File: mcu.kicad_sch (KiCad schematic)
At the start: 11 parts, among them J301 Conn_01x05_Pin, J302 Conn_01x10_Pin, SW301 TS-1088R-02026, SW302 TS-1088R-02026, U301 ESP-12F

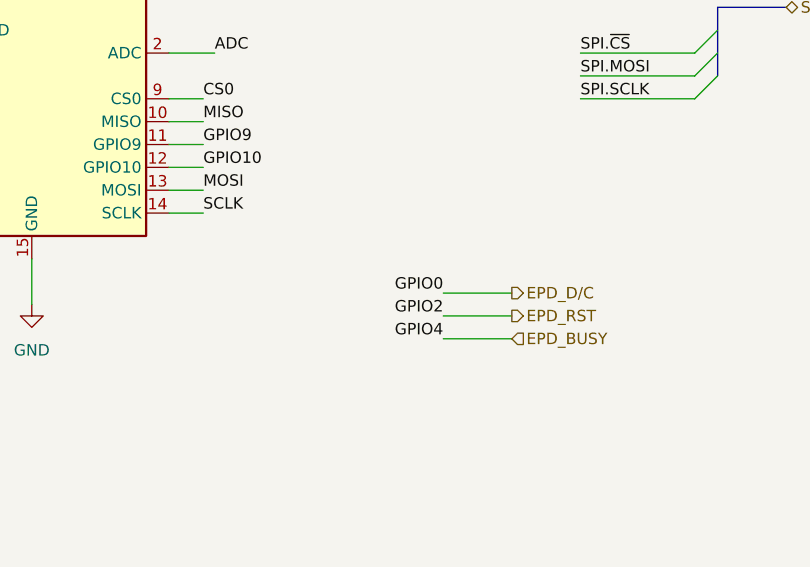
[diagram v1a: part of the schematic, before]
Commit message: Fix using same GPIO for epd D/C and boot
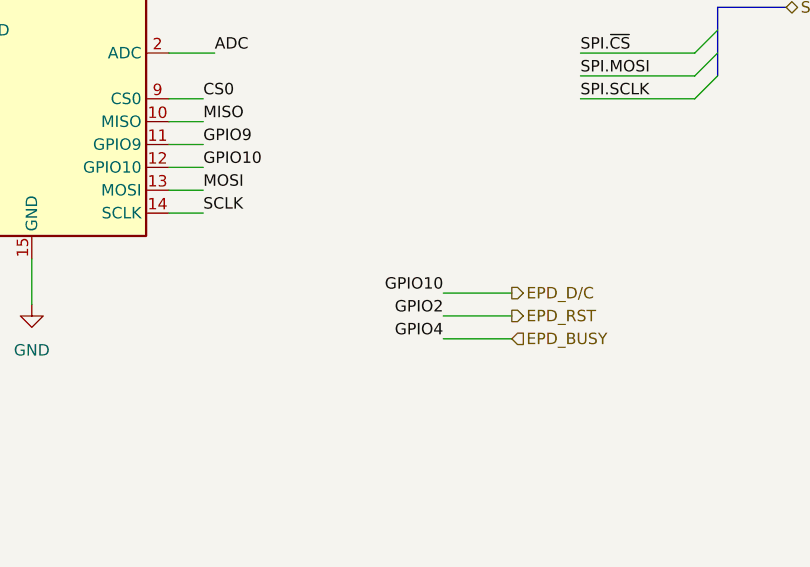
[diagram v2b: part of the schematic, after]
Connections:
- net GPIO10 is gone; now on net EPD_D/C: J302.10 (Pin_10), U301.12 (GPIO10)
- net EPD_D/C: no longer J302.6 (Pin_6), R302.2, SW302.2, U301.18 (GPIO0)
- new net GPIO0: J302.6 (Pin_6), R302.2, SW302.2, U301.18 (GPIO0)
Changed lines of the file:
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@@
 		)
 	)
-	(label "GPIO0"
+	(label "GPIO10"
 		(at 205.74 125.73 180)
 		(effects

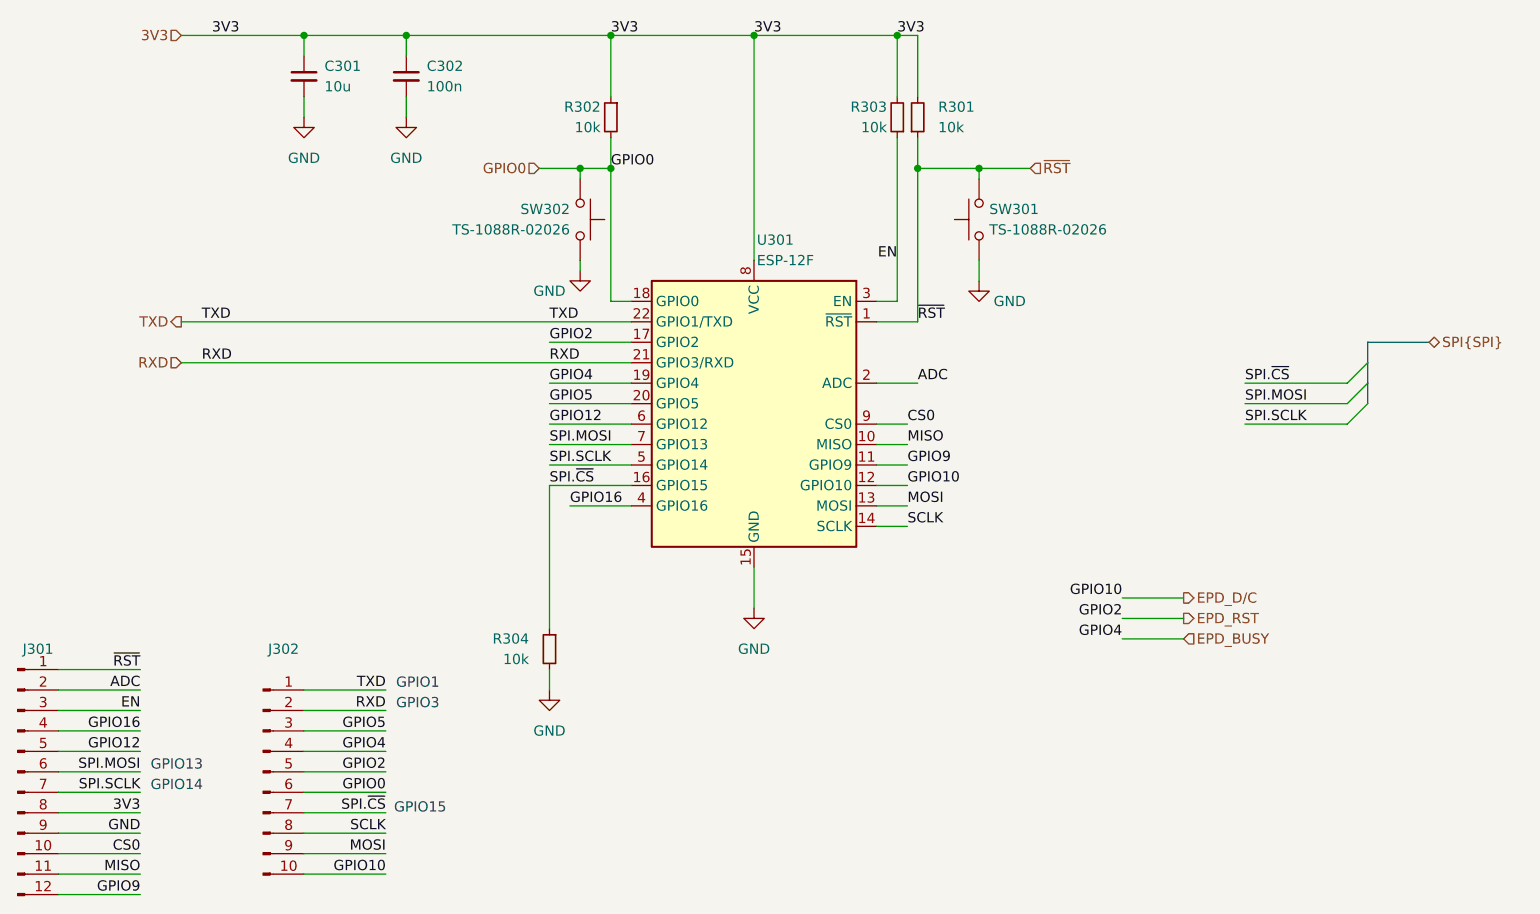
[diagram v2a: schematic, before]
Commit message: Update reference designators to single digit
Fits on the silk better
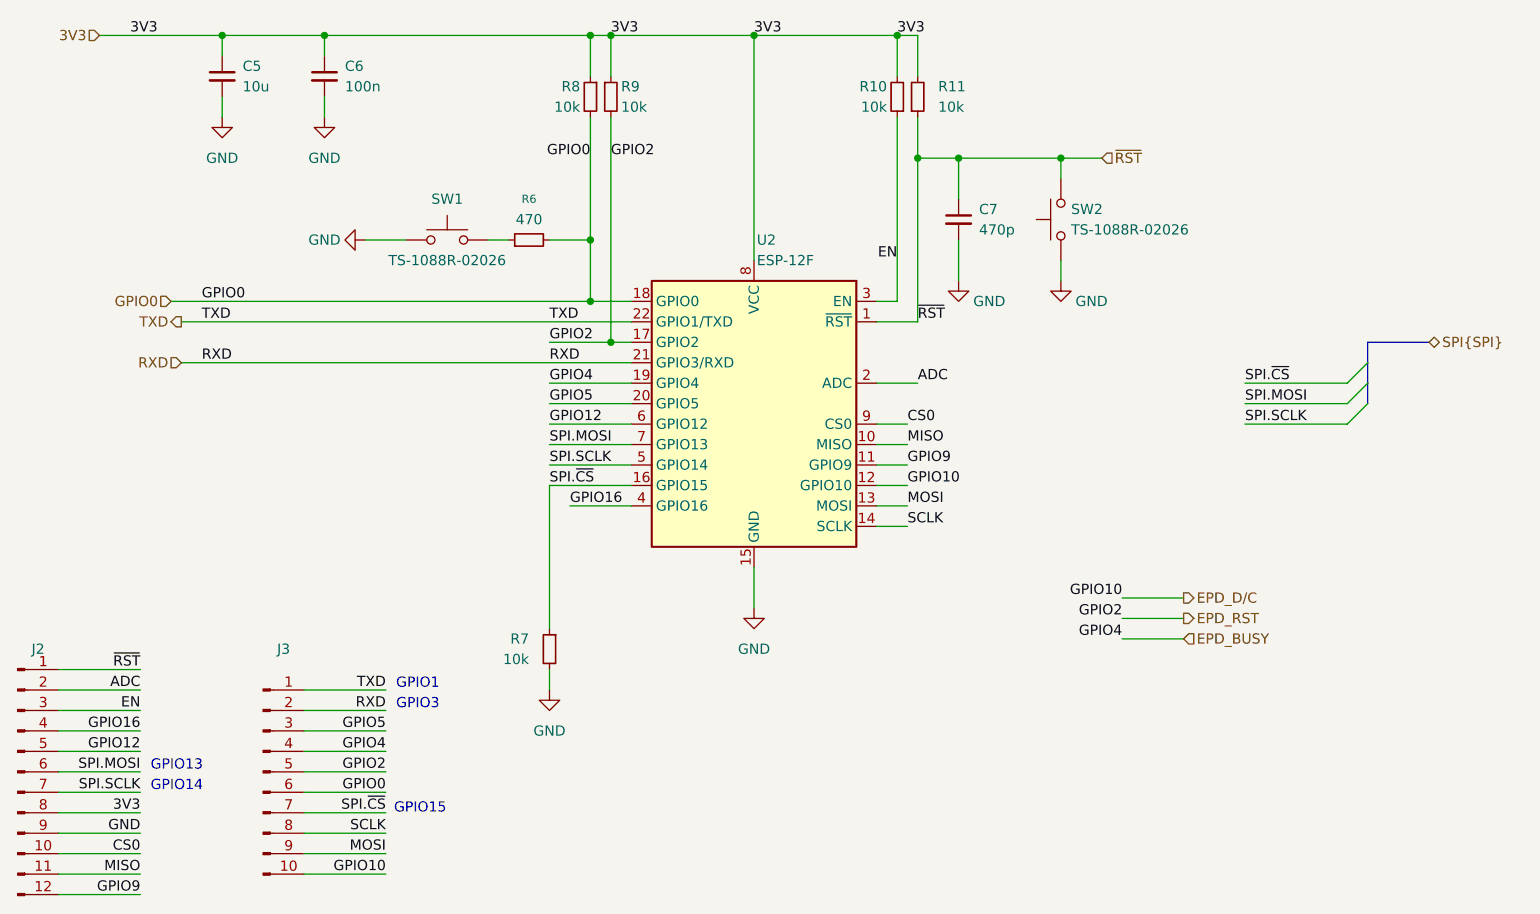
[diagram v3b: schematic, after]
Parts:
- added C7: 470p, Capacitor_SMD:C_0805_2012Metric, symbol Device:C_Small
- added R6: 470, Resistor_SMD:R_0805_2012Metric, symbol Device:R_Small
- added R9: 10k, Resistor_SMD:R_0805_2012Metric, symbol Device:R_Small
- renumbered C301 to C5, C302 to C6, J301 to J2, J302 to J3, R303 to R10, R301 to R11, R304 to R7, R302 to R8, SW302 to SW1, SW301 to SW2, U301 to U2
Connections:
- net 3V3: now also R9.1
- net EPD_RST: now also R9.2
- net GND: now also SW1.2, C7.2; no longer SW1.1
- net GPIO0: now also R6.2; no longer SW1.2
- net ~{RST}: now also C7.1
- new net: R6.1, SW1.1
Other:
- moved on the sheet: C5, C6, R10, R11, R8, SW1, SW2

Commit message: Lighthouse
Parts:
- SW1, SW2: footprint youdbetterrun:TS-1088R-02026_SW_SMD_3x4mm -> bedroom_lights:TS-1088R-02026_SW_SMD_3x4mm
- U2: symbol youdbetterrun:ESP-12F -> bedroom_lights:ESP-12F
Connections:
- net EPD_BUSY renamed GPIO4
- net EPD_D/C renamed CSO1
- net EPD_RST renamed GPIO2
- net GPIO12 renamed CSO2
- net GPIO16 renamed LSS2
- net GPIO9 renamed LSS1
- net SPI.MOSI renamed GPIO13
- net SPI.SCLK renamed GPIO14
- net SPI.~{CS} renamed GPIO15
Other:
- note removed: "GPIO13"
- note removed: "GPIO14"
- note removed: "GPIO15"
- company: (none) -> Marcel Robitaille
- title: (none) -> MCU

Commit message: ERC
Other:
- note added: "GPIO10"
- note added: "GPIO12"
- note added: "GPIO16"
- note added: "GPIO9"
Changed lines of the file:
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@@
 		(company "Marcel Robitaille")
+	)
+	(text "GPIO16"
+		(exclude_from_sim no)
+		(at 213.36 114.3 0)
+		(effects
+			(font
+				(size 1.27 1.27)
+			)
+			(justify left bottom)
+		)
 	)
 	(text "GPIO1"
@@
 		)
 	)
+	(text "GPIO10"
+		(exclude_from_sim no)
+		(at 213.36 104.14 0)
+		(effects
+			(font
+				(size 1.27 1.27)
+			)
+			(justify left bottom)
+		)
+	)
+	(text "GPIO12"
+		(exclude_from_sim no)
+		(at 213.36 106.68 0)
+		(effects
+			(font
+				(size 1.27 1.27)
+			)
+			(justify left bottom)
+		)
+	)
 	(text "GPIO3"
 		(exclude_from_sim no)
 		(at 115.57 139.7 0)
+		(effects
+			(font
+				(size 1.27 1.27)
+			)
+			(justify left bottom)
+		)
+	)
+	(text "GPIO9"
+		(exclude_from_sim no)
+		(at 213.36 111.76 0)
 		(effects
 			(font
@@
 	(wire
 		(pts
-			(xy 213.36 106.68) (xy 218.44 106.68)
+			(xy 213.36 106.68) (xy 223.52 106.68)
 		)
 		(stroke
@@
 	(wire
 		(pts
-			(xy 213.36 114.3) (xy 218.44 114.3)
+			(xy 213.36 114.3) (xy 223.52 114.3)
 		)
 		(stroke
@@
 	(wire
 		(pts
-			(xy 213.36 111.76) (xy 218.44 111.76)
+			(xy 213.36 111.76) (xy 223.52 111.76)
 		)
 		(stroke
@@
 	(wire
 		(pts
-			(xy 213.36 104.14) (xy 218.44 104.14)
+			(xy 213.36 104.14) (xy 223.52 104.14)
 		)
 		(stroke
@@
 		)
 	)
+	(label "LSS1"
+		(at 213.36 111.76 180)
+		(effects
+			(font
+				(size 1.27 1.27)
+			)
+			(justify right bottom)
+		)
+	)
 	(label "SCLK"
 		(at 179.07 116.84 0)
@@
 		)
 	)
-	(label "GPIO12"
-		(at 83.82 144.78 180)
+	(label "CSO2"
+		(at 134.62 104.14 0)
+		(effects
+			(font
+				(size 1.27 1.27)
+			)
+			(justify left bottom)
+		)
+	)
+	(label "CSO1"
+		(at 114.3 160.02 180)
 		(effects
 			(font
@@
 		)
 	)
+	(label "CSO1"
+		(at 179.07 111.76 0)
+		(effects
+			(font
+				(size 1.27 1.27)
+			)
+			(justify left bottom)
+		)
+	)
 	(label "~{RST}"
 		(at 180.34 91.44 0)
@@
 		)
 	)
-	(label "GPIO12"
-		(at 134.62 104.14 0)
-		(effects
-			(font
-				(size 1.27 1.27)
-			)
-			(justify left bottom)
-		)
-	)
 	(label "GPIO2"
 		(at 142.24 71.12 0)
@@
 		)
 	)
+	(label "CSO2"
+		(at 83.82 144.78 180)
+		(effects
+			(font
+				(size 1.27 1.27)
+			)
+			(justify right bottom)
+		)
+	)
 	(label "MOSI"
 		(at 114.3 157.48 180)
@@
 		)
 	)
-	(label "GPIO9"
-		(at 213.36 111.76 180)
-		(effects
-			(font
-				(size 1.27 1.27)
-			)
-			(justify right bottom)
-		)
-	)
 	(label "3V3"
 		(at 83.82 152.4 180)
@@
 		)
 	)
-	(label "GPIO12"
-		(at 213.36 106.68 180)
-		(effects
-			(font
-				(size 1.27 1.27)
-			)
-			(justify right bottom)
-		)
-	)
 	(label "GPIO5"
 		(at 134.62 101.6 0)
@@
 		)
 	)
+	(label "LSS2"
+		(at 137.16 114.3 0)
+		(effects
+			(font
+				(size 1.27 1.27)
+			)
+			(justify left bottom)
+		)
+	)
+	(label "LSS2"
+		(at 213.36 114.3 180)
+		(effects
+			(font
+				(size 1.27 1.27)
+			)
+			(justify right bottom)
+		)
+	)
 	(label "3V3"
 		(at 82.55 55.88 0)
@@
 		)
 	)
-	(label "GPIO10"
-		(at 114.3 160.02 180)
-		(effects
-			(font
-				(size 1.27 1.27)
-			)
-			(justify right bottom)
-		)
-	)
 	(label "GPIO13"
 		(at 83.82 147.32 180)
@@
 		)
 	)
+	(label "LSS2"
+		(at 83.82 142.24 180)
+		(effects
+			(font
+				(size 1.27 1.27)
+			)
+			(justify right bottom)
+		)
+	)
 	(label "CS0"
 		(at 179.07 104.14 0)
@@
 		)
 	)
-	(label "GPIO9"
-		(at 179.07 109.22 0)
-		(effects
-			(font
-				(size 1.27 1.27)
-			)
-			(justify left bottom)
-		)
-	)
 	(label "GND"
 		(at 83.82 154.94 180)
@@
 		)
 	)
-	(label "GPIO9"
-		(at 83.82 162.56 180)
-		(effects
-			(font
-				(size 1.27 1.27)
-			)
-			(justify right bottom)
-		)
-	)
-	(label "GPIO16"
-		(at 213.36 114.3 180)
-		(effects
-			(font
-				(size 1.27 1.27)
-			)
-			(justify right bottom)
-		)
-	)
-	(label "GPIO16"
-		(at 83.82 142.24 180)
+	(label "CSO1"
+		(at 213.36 104.14 180)
 		(effects
 			(font
@@
 		)
 	)
+	(label "CSO2"
+		(at 213.36 106.68 180)
+		(effects
+			(font
+				(size 1.27 1.27)
+			)
+			(justify right bottom)
+		)
+	)
 	(label "MISO"
 		(at 83.82 160.02 180)
@@
 		)
 	)
+	(label "LSS1"
+		(at 83.82 162.56 180)
+		(effects
+			(font
+				(size 1.27 1.27)
+			)
+			(justify right bottom)
+		)
+	)
 	(label "TXD"
 		(at 134.62 91.44 0)
@@
 		)
 	)
-	(label "GPIO10"
-		(at 179.07 111.76 0)
-		(effects
-			(font
-				(size 1.27 1.27)
-			)
-			(justify left bottom)
-		)
-	)
 	(label "GPIO5"
 		(at 114.3 142.24 180)
@@
 		)
 	)
-	(label "GPIO10"
-		(at 213.36 104.14 180)
-		(effects
-			(font
-				(size 1.27 1.27)
-			)
-			(justify right bottom)
-		)
-	)
 	(label "GPIO0"
 		(at 91.44 88.9 0)
@@
 		)
 	)
-	(label "GPIO16"
-		(at 137.16 114.3 0)
-		(effects
-			(font
-				(size 1.27 1.27)
-			)
-			(justify left bottom)
-		)
-	)
 	(label "GPIO14"
 		(at 134.62 109.22 0)
@@
 		)
 	)
+	(label "LSS1"
+		(at 179.07 109.22 0)
+		(effects
+			(font
+				(size 1.27 1.27)
+			)
+			(justify left bottom)
+		)
+	)
 	(label "CS0"
 		(at 83.82 157.48 180)
@@
 	(hierarchical_label "LSS1"
 		(shape output)
-		(at 218.44 111.76 0)
+		(at 223.52 111.76 0)
 		(effects
 			(font
@@
 	(hierarchical_label "LSS2"
 		(shape output)
-		(at 218.44 114.3 0)
+		(at 223.52 114.3 0)
 		(effects
 			(font
@@
 	(hierarchical_label "CSO1"
 		(shape output)
-		(at 218.44 104.14 0)
+		(at 223.52 104.14 0)
 		(effects
 			(font
@@
 	(hierarchical_label "CSO2"
 		(shape output)
-		(at 218.44 106.68 0)
-		(effects
-			(font
+		(at 223.52 106.68 0)
+		(effects
+			(font

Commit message: Renamifications
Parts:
- SW1, SW2: footprint bedroom_lights:TS-1088R-02026_SW_SMD_3x4mm -> lighthouse:TS-1088R-02026_SW_SMD_3x4mm
- U2: symbol bedroom_lights:ESP-12F -> lighthouse:ESP-12F
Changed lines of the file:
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@@
 		)
 		(instances
-			(project "bedroom_lights"
+			(project "lighthouse"
 				(path "/50da2b4e-34b1-4787-8ee6-5d7d17f804f4/81f185f6-8abd-42b2-b2d9-f7e00f67ab8b"
 					(reference "#PWR010")
@@
 		)
 		(instances
-			(project "bedroom_lights"
+			(project "lighthouse"
 				(path "/50da2b4e-34b1-4787-8ee6-5d7d17f804f4/81f185f6-8abd-42b2-b2d9-f7e00f67ab8b"
 					(reference "#PWR012")
@@
 		)
 		(instances
-			(project "bedroom_lights"
+			(project "lighthouse"
 				(path "/50da2b4e-34b1-4787-8ee6-5d7d17f804f4/81f185f6-8abd-42b2-b2d9-f7e00f67ab8b"
 					(reference "#PWR014")
@@
 		)
 		(instances
-			(project "bedroom_lights"
+			(project "lighthouse"
 				(path "/50da2b4e-34b1-4787-8ee6-5d7d17f804f4/81f185f6-8abd-42b2-b2d9-f7e00f67ab8b"
 					(reference "C6")
@@
 		)
 		(instances
-			(project "bedroom_lights"
+			(project "lighthouse"
 				(path "/50da2b4e-34b1-4787-8ee6-5d7d17f804f4/81f185f6-8abd-42b2-b2d9-f7e00f67ab8b"
 					(reference "C5")
@@
 		)
 		(instances
-			(project "bedroom_lights"
+			(project "lighthouse"
 				(path "/50da2b4e-34b1-4787-8ee6-5d7d17f804f4/81f185f6-8abd-42b2-b2d9-f7e00f67ab8b"
 					(reference "#PWR013")
@@
 		)
 		(instances
-			(project "bedroom_lights"
+			(project "lighthouse"
 				(path "/50da2b4e-34b1-4787-8ee6-5d7d17f804f4/81f185f6-8abd-42b2-b2d9-f7e00f67ab8b"
 					(reference "J3")
@@
 		)
 		(instances
-			(project "bedroom_lights"
+			(project "lighthouse"
 				(path "/50da2b4e-34b1-4787-8ee6-5d7d17f804f4/81f185f6-8abd-42b2-b2d9-f7e00f67ab8b"
 					(reference "J2")
@@
 		)
 		(instances
-			(project "bedroom_lights"
+			(project "lighthouse"
 				(path "/50da2b4e-34b1-4787-8ee6-5d7d17f804f4/81f185f6-8abd-42b2-b2d9-f7e00f67ab8b"
 					(reference "R7")
@@
 		)
 		(instances
-			(project "bedroom_lights"
+			(project "lighthouse"
 				(path "/50da2b4e-34b1-4787-8ee6-5d7d17f804f4/81f185f6-8abd-42b2-b2d9-f7e00f67ab8b"
 					(reference "#PWR09")
@@
 		)
 		(instances
-			(project "bedroom_lights"
+			(project "lighthouse"
 				(path "/50da2b4e-34b1-4787-8ee6-5d7d17f804f4/81f185f6-8abd-42b2-b2d9-f7e00f67ab8b"
 					(reference "R8")
@@
 		)
 		(instances
-			(project "bedroom_lights"
+			(project "lighthouse"
 				(path "/50da2b4e-34b1-4787-8ee6-5d7d17f804f4/81f185f6-8abd-42b2-b2d9-f7e00f67ab8b"
 					(reference "#PWR015")
@@
 		)
 		(instances
-			(project "bedroom_lights"
+			(project "lighthouse"
 				(path "/50da2b4e-34b1-4787-8ee6-5d7d17f804f4/81f185f6-8abd-42b2-b2d9-f7e00f67ab8b"
 					(reference "#PWR011")
@@
 		)
 		(instances
-			(project "bedroom_lights"
+			(project "lighthouse"
 				(path "/50da2b4e-34b1-4787-8ee6-5d7d17f804f4/81f185f6-8abd-42b2-b2d9-f7e00f67ab8b"
 					(reference "R10")
@@
 	)
 	(symbol
-		(lib_id "bedroom_lights:ESP-12F")
+		(lib_id "lighthouse:ESP-12F")
 		(at 160.02 104.14 0)
 		(mirror y)
@@
 		)
 		(instances
-			(project "bedroom_lights"
+			(project "lighthouse"
 				(path "/50da2b4e-34b1-4787-8ee6-5d7d17f804f4/81f185f6-8abd-42b2-b2d9-f7e00f67ab8b"
 					(reference "U2")
@@
 		)
 		(instances
-			(project "bedroom_lights"
+			(project "lighthouse"
 				(path "/50da2b4e-34b1-4787-8ee6-5d7d17f804f4/81f185f6-8abd-42b2-b2d9-f7e00f67ab8b"
 					(reference "R9")
@@
 			)
 		)
-		(property "Footprint" "bedroom_lights:TS-1088R-02026_SW_SMD_3x4mm"
+		(property "Footprint" "lighthouse:TS-1088R-02026_SW_SMD_3x4mm"
 			(at 121.92 76.2 0)
 			(effects
@@
 		)
 		(instances
-			(project "bedroom_lights"
+			(project "lighthouse"
 				(path "/50da2b4e-34b1-4787-8ee6-5d7d17f804f4/81f185f6-8abd-42b2-b2d9-f7e00f67ab8b"
 					(reference "SW1")
@@
 		)
 		(instances
-			(project "bedroom_lights"
+			(project "lighthouse"
 				(path "/50da2b4e-34b1-4787-8ee6-5d7d17f804f4/81f185f6-8abd-42b2-b2d9-f7e00f67ab8b"
 					(reference "R11")
@@
 			)
 		)
-		(property "Footprint" "bedroom_lights:TS-1088R-02026_SW_SMD_3x4mm"
+		(property "Footprint" "lighthouse:TS-1088R-02026_SW_SMD_3x4mm"
 			(at 193.04 78.74 0)
 			(effects
@@
 		)
 		(instances
-			(project "bedroom_lights"
+			(project "lighthouse"
 				(path "/50da2b4e-34b1-4787-8ee6-5d7d17f804f4/81f185f6-8abd-42b2-b2d9-f7e00f67ab8b"
 					(reference "SW2")

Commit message: Add component attributes
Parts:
- C5: LCSC Part Number C5189822 -> (none); MPN CS2012X7R106M100NRE -> CL21A106KOQNNNE; Manufacturer Samwha Capacitor -> Samsung Electro-Mechanics; Mouser Part Number (none) -> 187-CL21A106KOQNNNE; Rated Voltage 10V -> 16V; Tolerance 20% -> 10%
- C7: MPN (none) -> 885012007038; Manufacturer (none) -> Wurth Elektronik; Mouser Part Number (none) -> 710-885012007038
- R10, R11, R7, R8, R9: LCSC Part Number C17414 -> (none); MPN 0805W8F1002T5E -> CRCW080510K0JNEAC; Manufacturer UNI-ROYAL(Uniroyal Elec) -> Vishay; Mouser Part Number (none) -> 71-CRCW080510K0JNEAC; Tolerance 1% -> 5 %
- R6: MPN (none) -> CRCW0805470RFKEA; Manufacturer (none) -> Vishay; Mouser Part Number (none) -> 71-CRCW0805-470-E3; Package (none) -> 0805; Power (none) -> 250 mW; Tolerance (none) -> 1%
